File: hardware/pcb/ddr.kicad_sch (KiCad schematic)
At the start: 0 parts

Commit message: replaced footprint with one fron cse
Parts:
- added U3: K4E6E304EC-EGCG, K4E6E304EC-EGCG:FBGA-178_L11.5-W11.0_K4E6E304EC-TL, symbol K4E6E304EC-EGCG:K4E6E304EC-EGCG
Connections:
- new net: U3.A1 (DNU), U3.A12 (DNU), U3.A13 (DNU), U3.A2 (DNU), U3.B1 (DNU), U3.B13 (DNU), U3.T1 (DNU), U3.T13 (DNU), U3.U1 (DNU), U3.U12 (DNU), U3.U13 (DNU), U3.U2 (DNU)
- new net: U3.K9 (NC), U3.R3 (NC)
- new net VSS: U3.R4 (VSS), U3.R5 (VSS)
- new net VSSQ: U3.B12 (VSSQ), U3.B6 (VSSQ), U3.C6 (VSSQ), U3.D12 (VSSQ), U3.E6 (VSSQ), U3.F12 (VSSQ), U3.F6 (VSSQ), U3.G6 (VSSQ), U3.G9 (VSSQ), U3.H10 (VSSQ), U3.K10 (VSSQ), U3.L9 (VSSQ), U3.M12 (VSSQ), U3.M6 (VSSQ), U3.N6 (VSSQ), U3.P12 (VSSQ), U3.R6 (VSSQ), U3.T12 (VSSQ), U3.T6 (VSSQ)

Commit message: finished ddr symbol
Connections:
- net VSS is gone; now on net GND: U3.R4 (VSS), U3.R5 (VSS)
- net VSSQ is gone; now on net GND: U3.B12 (VSSQ), U3.B6 (VSSQ), U3.C6 (VSSQ), U3.D12 (VSSQ), U3.E6 (VSSQ), U3.F12 (VSSQ), U3.F6 (VSSQ), U3.G6 (VSSQ), U3.G9 (VSSQ), U3.H10 (VSSQ), U3.K10 (VSSQ), U3.L9 (VSSQ), U3.M12 (VSSQ), U3.M6 (VSSQ), U3.N6 (VSSQ), U3.P12 (VSSQ), U3.R6 (VSSQ), U3.T12 (VSSQ), U3.T6 (VSSQ)
- net VDD1: now reaches U3.A10 (VDD1)
- net VDD1: now also U3.A3 (VDD1), U3.A4 (VDD1), U3.A5 (VDD1), U3.A6 (VDD1), U3.U10 (VDD1), U3.U3 (VDD1), U3.U4 (VDD1), U3.U5 (VDD1), U3.U6 (VDD1)
- net VDD2: now reaches U3.A11 (VDDQ)
- net VDD2: now also U3.A8 (VDD2), U3.A9 (VDD2), U3.C12 (VDDQ), U3.D4 (VDD2), U3.D5 (VDD2), U3.D6 (VDD2), U3.E12 (VDDQ), U3.E8 (VDDQ), U3.F2 (VDDCA), U3.G12 (VDDQ), U3.G2 (VDDCA), U3.G5 (VDD2), U3.H11 (VDDQ), U3.H12 (VDDQ), U3.H3 (VDDCA), U3.H5 (VDD2), U3.H6 (VDD2), U3.H8 (VDDQ), U3.H9 (VDDQ), U3.J10 (VDDQ), U3.J5 (VDD2), U3.J6 (VDD2), U3.J9 (VDDQ), U3.K11 (VDDQ), U3.K12 (VDD2), U3.K5 (VDD2), U3.K6 (VDD2), U3.K8 (VDDQ), U3.L12 (VDDQ), U3.L2 (VDDCA), U3.L5 (VDD2), U3.M2 (VDDCA), U3.N12 (VDDQ), U3.N8 (VDDQ), U3.P4 (VDD2), U3.P5 (VDD2), U3.P6 (VDD2), U3.R12 (VDDQ), U3.U11 (VDDQ), U3.U8 (VDD2), U3.U9 (VDD2)
- net GND: now reaches U3.B2 (VSS)
- net GND: now also U3.B5 (VSS), U3.C3 (VSSCA), U3.C5 (VSS), U3.D3 (VSSCA), U3.E4 (VSS), U3.E5 (VSS), U3.F4 (VSSCA), U3.F5 (VSS), U3.G3 (VSSCA), U3.G4 (VSSCA), U3.H2 (VSS), U3.J12 (VSS), U3.J4 (VSSCA), U3.K2 (VSS), U3.L6 (VSS), U3.M4 (VSSCA), U3.M5 (VSS), U3.N4 (VSS), U3.N5 (VSS), U3.P3 (VSSCA), U3.T2 (VSS), U3.T3 (VSS), U3.T4 (VSS), U3.T5 (VSS)
- net at U3.B4 (NC): now also U3.C4 (NC), U3.K9 (NC), U3.R3 (NC)
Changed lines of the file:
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@@
 	(generator_version "10.0")
 	(paper "A4")
+	(junction
+		(at 135.89 33.02)
+		(diameter 0)
+		(color 0 0 0 0)
+	)
+	(junction
+		(at 137.16 138.43)
+		(diameter 0)
+		(color 0 0 0 0)
+	)
+	(wire
+		(pts
+			(xy 134.62 137.16) (xy 134.62 138.43)
+		)
+		(stroke
+			(width 0)
+			(type default)
+		)
+	)
+	(wire
+		(pts
+			(xy 139.7 138.43) (xy 137.16 138.43)
+		)
+		(stroke
+			(width 0)
+			(type default)
+		)
+	)
+	(wire
+		(pts
+			(xy 134.62 138.43) (xy 137.16 138.43)
+		)
+		(stroke
+			(width 0)
+			(type default)
+		)
+	)
+	(wire
+		(pts
+			(xy 135.89 33.02) (xy 138.43 33.02)
+		)
+		(stroke
+			(width 0)
+			(type default)
+		)
+	)
+	(wire
+		(pts
+			(xy 133.35 33.02) (xy 135.89 33.02)
+		)
+		(stroke
+			(width 0)
+			(type default)
+		)
+	)
+	(wire
+		(pts
+			(xy 139.7 137.16) (xy 139.7 138.43)
+		)
+		(stroke
+			(width 0)
+			(type default)
+		)
+	)
+	(wire
+		(pts
+			(xy 137.16 137.16) (xy 137.16 138.43)
+		)
+		(stroke
+			(width 0)
+			(type default)
+		)
 	)
 	(symbol
 		(lib_id "K4E6E304EC-EGCG:K4E6E304EC-EGCG")
-		(at 30.48 68.58 0)
+		(at 137.16 85.09 0)
 		(unit 1)
 		(body_style 1)
@@
 		(fields_autoplaced yes)
 		(property "Reference" "U3"
-			(at 26.035 -49.53 0)
+			(at 132.715 -33.02 0)
 			(show_name no)
 			(do_not_autoplace no)
@@
 		)
 		(property "Value" "K4E6E304EC-EGCG"
-			(at 26.035 -46.99 0)
+			(at 132.715 -30.48 0)
 			(show_name no)
 			(do_not_autoplace no)
@@
 		)
 		(property "Footprint" "K4E6E304EC-EGCG:FBGA-178_L11.5-W11.0_K4E6E304EC-TL"
-			(at 30.48 187.96 0)
+			(at 137.16 204.47 0)
 			(hide yes)
 			(show_name no)
@@
 		)
 		(property "Datasheet" "https://www.lcsc.com/datasheet/C2803256.pdf"
-			(at 30.48 190.5 0)
+			(at 137.16 207.01 0)
 			(hide yes)
 			(show_name no)
@@
 		)
 		(property "Description" ""
-			(at 30.48 68.58 0)
+			(at 137.16 85.09 0)
 			(hide yes)
 			(show_name no)
@@
 		)
 		(property "Manufacturer" "SAMSUNG(三星半导体)"
-			(at 30.48 193.04 0)
+			(at 137.16 209.55 0)
 			(hide yes)
 			(show_name no)
@@
 		)
 		(property "MPN" "K4E6E304EC-EGCG"
-			(at 30.48 195.58 0)
+			(at 137.16 212.09 0)
 			(hide yes)
 			(show_name no)
@@
 		)
 		(property "LCSC Part" "C2803256"
-			(at 30.48 198.12 0)
+			(at 137.16 214.63 0)
 			(hide yes)
 			(show_name no)
@@
 					(unit 1)
 				)
+			)
+		)
+	)
+	(symbol
+		(lib_id "power:GND")
+		(at 137.16 138.43 0)
+		(unit 1)
+		(body_style 1)
+		(exclude_from_sim no)
+		(in_bom yes)
+		(on_board yes)
+		(in_pos_files yes)
+		(dnp no)
+		(fields_autoplaced yes)
+		(property "Reference" "#PWR01"
+			(at 137.16 144.78 0)
+			(hide yes)
+			(show_name no)
+			(do_not_autoplace no)
+			(effects
+				(font
+					(size 1.27 1.27)
+				)
+			)
+		)
+		(property "Value" "GND"
+			(at 137.16 143.51 0)
+			(show_name no)
+			(do_not_autoplace no)
+			(effects
+				(font
+					(size 1.27 1.27)
+				)
+			)
+		)
+		(property "Footprint" ""
+			(at 137.16 138.43 0)
+			(hide yes)
+			(show_name no)
+			(do_not_autoplace no)
+			(effects
+				(font
+					(size 1.27 1.27)
+				)
+			)
+		)
+		(property "Datasheet" ""
+			(at 137.16 138.43 0)
+			(hide yes)
+			(show_name no)
+			(do_not_autoplace no)
+			(effects
+				(font
+					(size 1.27 1.27)
+				)
+			)
+		)
+		(property "Description" "Power symbol creates a global label with name \"GND\" , ground"
+			(at 137.16 138.43 0)
+			(hide yes)
+			(show_name no)
+			(do_not_autoplace no)
+			(effects
+				(font
+					(size 1.27 1.27)
+				)
+			)
+		)
+		(pin "1"
+		)
+		(instances
+			(project "meko"
+				(path "/da54f10a-146b-4941-a9c7-55c7173bb101/6a1996a1-d776-4235-b4ef-703258aa0c56"
+					(reference "#PWR01")
+					(unit 1)
+				)

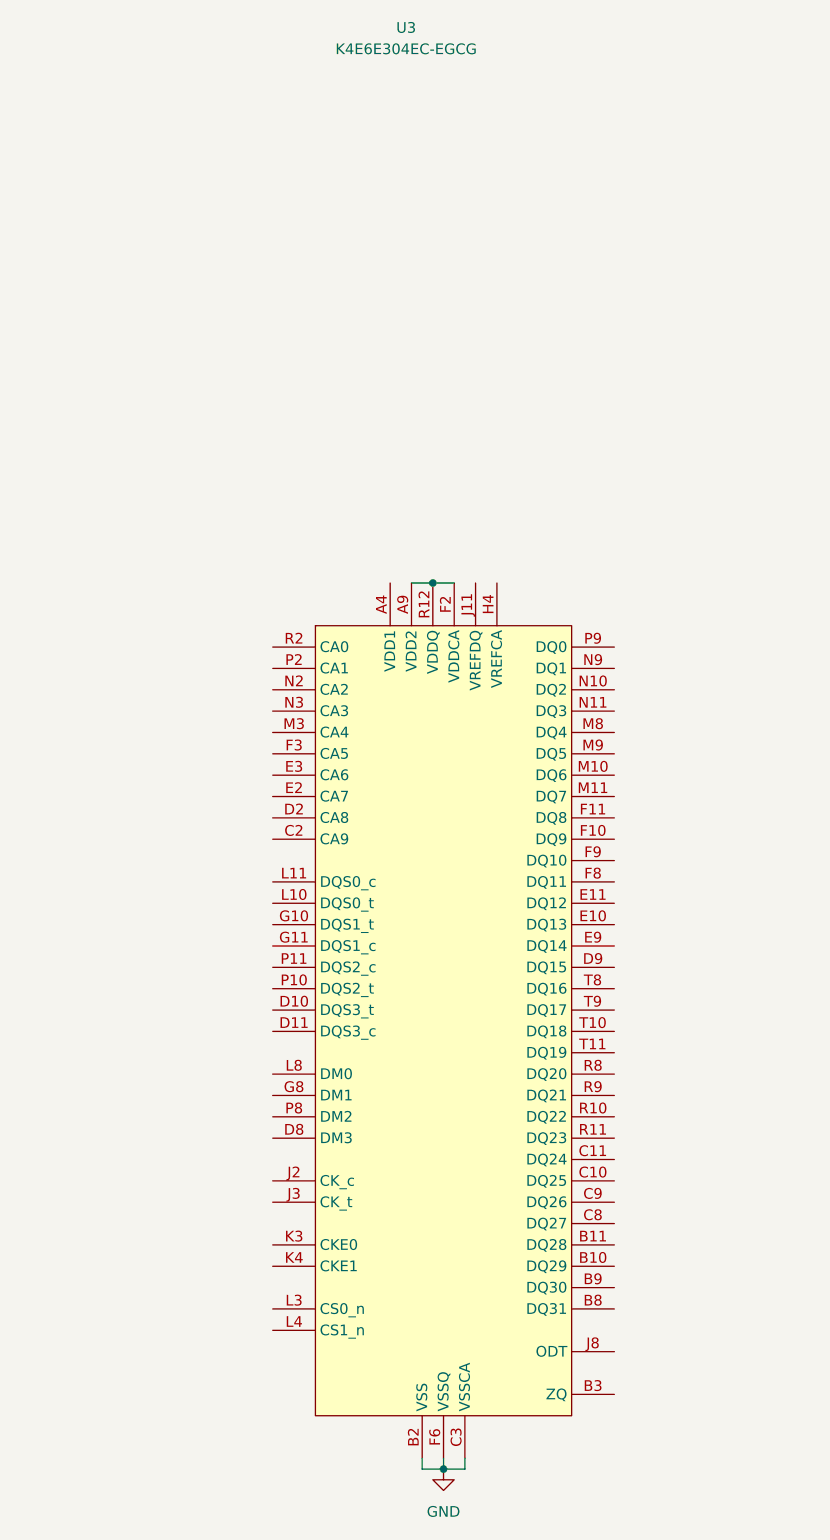
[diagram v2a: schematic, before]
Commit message: connected ddr to sama7, still need to do pwr
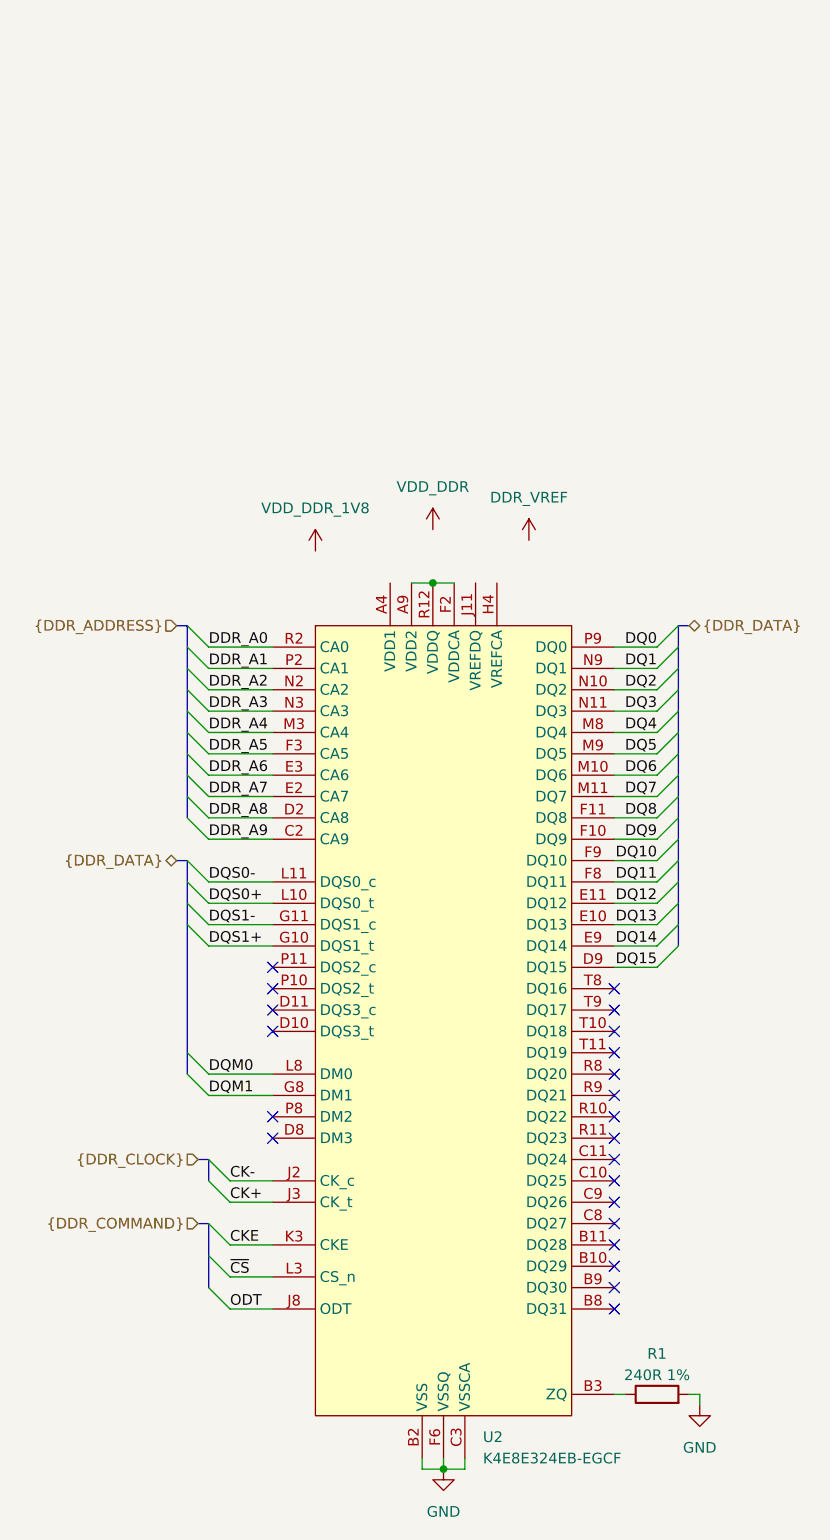
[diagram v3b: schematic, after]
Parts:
- removed U3: K4E6E304EC-EGCG, K4E6E304EC-EGCG:FBGA-178_L11.5-W11.0_K4E6E304EC-TL, symbol K4E6E304EC-EGCG:K4E6E304EC-EGCG
- added R1: 240R 1%, symbol Device:R
- added U2: K4E8E324EB-EGCF, K4E6E304EC-EGCG:FBGA-178_L11.5-W11.0_K4E6E304EC-TL, symbol K4E6E304EC-EGCG:K4E8E324EB-EGCF
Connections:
- net GND: now also R1.2, U2.B12 (VSSQ), U2.B2 (VSS), U2.B5 (VSS), U2.B6 (VSSQ), U2.C3 (VSSCA), U2.C5 (VSS), U2.C6 (VSSQ), U2.D12 (VSSQ), U2.D3 (VSSCA), U2.E4 (VSS), U2.E5 (VSS), U2.E6 (VSSQ), U2.F12 (VSSQ), U2.F4 (VSSCA), U2.F5 (VSS), U2.F6 (VSSQ), U2.G3 (VSSCA), U2.G4 (VSSCA), U2.G6 (VSSQ), U2.G9 (VSSQ), U2.H10 (VSSQ), U2.H2 (VSS), U2.J12 (VSS), U2.J4 (VSSCA), U2.K10 (VSSQ), U2.K2 (VSS), U2.L6 (VSS), U2.L9 (VSSQ), U2.M12 (VSSQ), U2.M4 (VSSCA), U2.M5 (VSS), U2.M6 (VSSQ), U2.N4 (VSS), U2.N5 (VSS), U2.N6 (VSSQ), U2.P12 (VSSQ), U2.P3 (VSSCA), U2.R4 (VSS), U2.R5 (VSS), U2.R6 (VSSQ), U2.T12 (VSSQ), U2.T2 (VSS), U2.T3 (VSS), U2.T4 (VSS), U2.T5 (VSS), U2.T6 (VSSQ)
- net VDD1: now also U2.A10 (VDD1), U2.A3 (VDD1), U2.A4 (VDD1), U2.A5 (VDD1), U2.A6 (VDD1), U2.U10 (VDD1), U2.U3 (VDD1), U2.U4 (VDD1), U2.U5 (VDD1), U2.U6 (VDD1)
- net VDD2: now also U2.A11 (VDDQ), U2.A8 (VDD2), U2.A9 (VDD2), U2.C12 (VDDQ), U2.D4 (VDD2), U2.D5 (VDD2), U2.D6 (VDD2), U2.E12 (VDDQ), U2.E8 (VDDQ), U2.F2 (VDDCA), U2.G12 (VDDQ), U2.G2 (VDDCA), U2.G5 (VDD2), U2.H11 (VDDQ), U2.H12 (VDDQ), U2.H3 (VDDCA), U2.H5 (VDD2), U2.H6 (VDD2), U2.H8 (VDDQ), U2.H9 (VDDQ), U2.J10 (VDDQ), U2.J5 (VDD2), U2.J6 (VDD2), U2.J9 (VDDQ), U2.K11 (VDDQ), U2.K12 (VDD2), U2.K5 (VDD2), U2.K6 (VDD2), U2.K8 (VDDQ), U2.L12 (VDDQ), U2.L2 (VDDCA), U2.L5 (VDD2), U2.M2 (VDDCA), U2.N12 (VDDQ), U2.N8 (VDDQ), U2.P4 (VDD2), U2.P5 (VDD2), U2.P6 (VDD2), U2.R12 (VDDQ), U2.U11 (VDDQ), U2.U8 (VDD2), U2.U9 (VDD2)
- new net: R1.1, U2.B3 (ZQ)
- new net: U2.A1 (DNU), U2.A12 (DNU), U2.A13 (DNU), U2.A2 (DNU), U2.B1 (DNU), U2.B13 (DNU), U2.T1 (DNU), U2.T13 (DNU), U2.U1 (DNU), U2.U12 (DNU), U2.U13 (DNU), U2.U2 (DNU)
- new net: U2.B4 (NC), U2.C4 (NC), U2.K9 (NC), U2.L4 (NC), U2.R3 (NC)
- new net CK+: U2.J3 (CK_t)
- new net CK-: U2.J2 (CK_c)
- new net CKE: U2.K3 (CKE)
- new net DDR_A0: U2.R2 (CA0)
- new net DDR_A1: U2.P2 (CA1)
- new net DDR_A2: U2.N2 (CA2)
- new net DDR_A3: U2.N3 (CA3)
- new net DDR_A4: U2.M3 (CA4)
- new net DDR_A5: U2.F3 (CA5)
- new net DDR_A6: U2.E3 (CA6)
- new net DDR_A7: U2.E2 (CA7)
- new net DDR_A8: U2.D2 (CA8)
- new net DDR_A9: U2.C2 (CA9)
- new net DQ0: U2.P9 (DQ0)
- new net DQ1: U2.N9 (DQ1)
- new net DQ10: U2.F9 (DQ10)
- new net DQ11: U2.F8 (DQ11)
- new net DQ12: U2.E11 (DQ12)
- new net DQ13: U2.E10 (DQ13)
- new net DQ14: U2.E9 (DQ14)
- new net DQ15: U2.D9 (DQ15)
- new net DQ2: U2.N10 (DQ2)
- new net DQ3: U2.N11 (DQ3)
- new net DQ4: U2.M8 (DQ4)
- new net DQ5: U2.M9 (DQ5)
- new net DQ6: U2.M10 (DQ6)
- new net DQ7: U2.M11 (DQ7)
- new net DQ8: U2.F11 (DQ8)
- new net DQ9: U2.F10 (DQ9)
- new net DQM0: U2.L8 (DM0)
- new net DQM1: U2.G8 (DM1)
- new net DQS0+: U2.L10 (DQS0_t)
- new net DQS0-: U2.L11 (DQS0_c)
- new net DQS1+: U2.G10 (DQS1_t)
- new net DQS1-: U2.G11 (DQS1_c)
- new net ODT: U2.J8 (ODT)
- new net ~{CS}: U2.L3 (CS_n)
- no-connect marks 0 -> 22

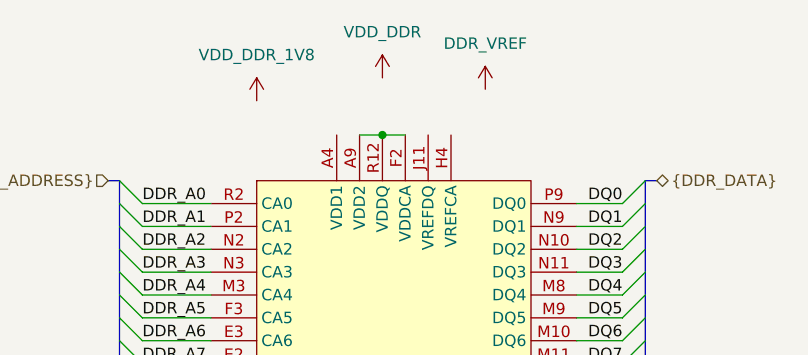
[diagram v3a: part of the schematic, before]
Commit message: started usb
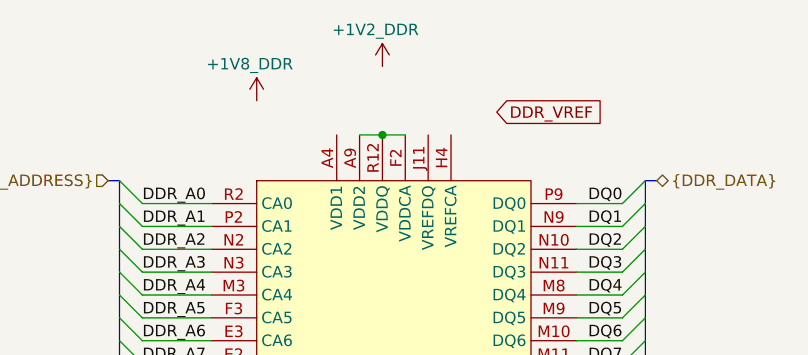
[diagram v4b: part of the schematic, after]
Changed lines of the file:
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@@
+		)
+	)
+	(global_label "DDR_VREF"
+		(shape input)
+		(at 148.59 30.48 0)
+		(fields_autoplaced yes)
+		(effects
+			(font
+				(size 1.27 1.27)
+			)
+			(justify left)
+		)
+		(property "Intersheetrefs" "${INTERSHEET_REFS}"
+			(at 160.949 30.48 0)
+			(hide yes)
+			(show_name no)
+			(do_not_autoplace no)
+			(effects
+				(font
+					(size 1.27 1.27)
+				)
+				(justify left)
+			)
 		)
 	)
@@
 				(path "/da54f10a-146b-4941-a9c7-55c7173bb101/6a1996a1-d776-4235-b4ef-703258aa0c56"
 					(reference "R1")
-					(unit 1)
-				)
-			)
-		)
-	)
-	(symbol
-		(lib_id "power:VDD")
-		(at 135.89 26.67 0)
-		(unit 1)
-		(body_style 1)
-		(exclude_from_sim no)
-		(in_bom yes)
-		(on_board yes)
-		(in_pos_files yes)
-		(dnp no)
-		(fields_autoplaced yes)
-		(property "Reference" "#PWR02"
-			(at 135.89 30.48 0)
-			(hide yes)
-			(show_name no)
-			(do_not_autoplace no)
-			(effects
-				(font
-					(size 1.27 1.27)
-				)
-			)
-		)
-		(property "Value" "VDD_DDR"
-			(at 135.89 21.59 0)
-			(show_name no)
-			(do_not_autoplace no)
-			(effects
-				(font
-					(size 1.27 1.27)
-				)
-			)
-		)
-		(property "Footprint" ""
-			(at 135.89 26.67 0)
-			(hide yes)
-			(show_name no)
-			(do_not_autoplace no)
-			(effects
-				(font
-					(size 1.27 1.27)
-				)
-			)
-		)
-		(property "Datasheet" ""
-			(at 135.89 26.67 0)
-			(hide yes)
-			(show_name no)
-			(do_not_autoplace no)
-			(effects
-				(font
-					(size 1.27 1.27)
-				)
-			)
-		)
-		(property "Description" "Power symbol creates a global label with name \"VDD\""
-			(at 135.89 26.67 0)
-			(hide yes)
-			(show_name no)
-			(do_not_autoplace no)
-			(effects
-				(font
-					(size 1.27 1.27)
-				)
-			)
-		)
-		(pin "1"
-		)
-		(instances
-			(project "meko"
-				(path "/da54f10a-146b-4941-a9c7-55c7173bb101/6a1996a1-d776-4235-b4ef-703258aa0c56"
-					(reference "#PWR02")
 					(unit 1)
 				)
@@
 	(symbol
 		(lib_id "power:VDD")
-		(at 147.32 27.94 0)
+		(at 135.89 25.4 0)
 		(unit 1)
 		(body_style 1)
@@
 		(in_pos_files yes)
 		(dnp no)
-		(fields_autoplaced yes)
-		(property "Reference" "#PWR04"
-			(at 147.32 31.75 0)
-			(hide yes)
-			(show_name no)
-			(do_not_autoplace no)
-			(effects
-				(font
-					(size 1.27 1.27)
-				)
-			)
-		)
-		(property "Value" "DDR_VREF"
-			(at 147.32 22.86 0)
-			(show_name no)
-			(do_not_autoplace no)
-			(effects
-				(font
-					(size 1.27 1.27)
-				)
+		(property "Reference" "#PWR07"
+			(at 135.89 29.21 0)
+			(hide yes)
+			(show_name no)
+			(do_not_autoplace no)
+			(effects
+				(font
+					(size 1.27 1.27)
+				)
+			)
+		)
+		(property "Value" "+1V2_DDR"
+			(at 130.302 21.336 0)
+			(show_name no)
+			(do_not_autoplace no)
+			(effects
+				(font
+					(size 1.27 1.27)
+				)
+				(justify left)
 			)
 		)
 		(property "Footprint" ""
-			(at 147.32 27.94 0)
+			(at 135.89 25.4 0)
 			(hide yes)
 			(show_name no)
@@
 		)
 		(property "Datasheet" ""
-			(at 147.32 27.94 0)
+			(at 135.89 25.4 0)
 			(hide yes)
 			(show_name no)
@@
 		)
 		(property "Description" "Power symbol creates a global label with name \"VDD\""
-			(at 147.32 27.94 0)
+			(at 135.89 25.4 0)
 			(hide yes)
 			(show_name no)
@@
 			(project "meko"
 				(path "/da54f10a-146b-4941-a9c7-55c7173bb101/6a1996a1-d776-4235-b4ef-703258aa0c56"
-					(reference "#PWR04")
+					(reference "#PWR07")
 					(unit 1)
 				)
@@
 		(in_pos_files yes)
 		(dnp no)
-		(fields_autoplaced yes)
 		(property "Reference" "#PWR03"
 			(at 121.92 33.02 0)
@@
 			)
 		)
-		(property "Value" "VDD_DDR_1V8"
-			(at 121.92 24.13 0)
-			(show_name no)
-			(do_not_autoplace no)
-			(effects
-				(font
-					(size 1.27 1.27)
-				)
-			)
-		)
+		(property "Value" "+1V8_DDR"
+			(at 116.332 25.146 0)
+			(show_name no)
+			(do_not_autoplace no)
+			(effects
+				(font
+					(size 1.27 1.27)
+				)
+				(justify left)
+			)
+		)

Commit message: finished power
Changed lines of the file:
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@@
 			)
 		)
-		(property "Value" "+1V8_DDR"
+		(property "Value" "+1V8"
 			(at 116.332 25.146 0)
 			(show_name no)

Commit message: contiunued working
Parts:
- U2: Manufacturer SAMSUNG -> (none)
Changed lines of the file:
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@@
+			)
+		)
+		(property "KLC_S3.3" ""
+			(at 162.56 129.54 90)
+			(hide yes)
+			(show_name no)
+			(do_not_autoplace no)
+			(effects
+				(font
+					(size 1.27 1.27)
+				)
+			)
+		)
+		(property "KLC_S4.1" ""
+			(at 162.56 129.54 90)
+			(hide yes)
+			(show_name no)
+			(do_not_autoplace no)
+			(effects
+				(font
+					(size 1.27 1.27)
+				)
 			)
 		)
@@
 			)
 		)
-		(property "Manufacturer" "SAMSUNG"
-			(at 137.16 248.158 0)
-			(hide yes)
-			(show_name no)
-			(do_not_autoplace no)
-			(effects
-				(font
-					(size 1.27 1.27)
-				)
-			)
-		)
 		(property "MPN" "K4E8E324EB-EGCF"
 			(at 137.16 250.698 0)
@@
 			(at 137.16 85.09 0)
 			(hide yes)
+			(show_name no)
+			(do_not_autoplace no)
+			(effects
+				(font
+					(size 1.27 1.27)
+				)
+			)
+		)
+		(property "KLC_S3.3" ""
+			(at 137.16 85.09 0)
+			(hide yes)
+			(show_name no)
+			(do_not_autoplace no)
+			(effects
+				(font
+					(size 1.27 1.27)
+				)
+			)
+		)
+		(property "KLC_S4.1" ""
+			(at 137.16 85.09 0)
+			(hide yes)

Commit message: small stuff with mpu
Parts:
- added C28, C29: 100n, symbol Device:C_Small
- added R11, R12: 1k ± 1%, symbol Device:R_Small
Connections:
- net +1V2_DDR: now also C28.2, R11.1
- net DDR_VREF: now also C28.1, C29.2, R11.2, R12.1
- net GND: now also C29.1, R12.2
- net at U2.H4 (VREFCA): now also U2.J11 (VREFDQ)

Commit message: bunch of small changes
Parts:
- R11, R12: value 1k ± 1% -> 1k
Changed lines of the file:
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@@
 			)
 		)
-		(property "Value" "1k ± 1%"
-			(at 199.644 54.356 0)
+		(property "Value" "1k"
+			(at 202.692 54.356 0)
 			(show_name no)
 			(do_not_autoplace no)
@@
 			)
 		)
-		(property "Value" "1k ± 1%"
-			(at 199.644 61.976 0)
-			(show_name no)
-			(do_not_autoplace no)
+		(property "Value" "1k"
+			(at 202.692 61.976 0)
+			(show_name no)
+			(do_not_autoplace no)
